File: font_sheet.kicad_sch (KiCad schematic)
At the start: 0 parts

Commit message: Troquei o micro para STM32H523, adicionei o cristal HSE, circuito da fonte de 5V e 3v3, CAN, SD
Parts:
- added C14, C15: 10u, Capacitor_THT:CP_Radial_D6.3mm_P2.50mm, symbol Device:C
- added C16: 10u, symbol Device:C
- added C17: 100n, symbol Device:C
- added D4: LED, BajaKICAD:LED_1210_HandSoldering, symbol Device:LED
- added R2: 1k, Resistor_SMD:R_1206_3216Metric_Pad1.30x1.75mm_HandSolder, symbol Device:R
- added U1: AMS1117-3.3, Package_TO_SOT_SMD:SOT-223-3_TabPin2, symbol Regulator_Linear:AMS1117-3.3
- added U11: AMS1117-5.0, Package_TO_SOT_SMD:SOT-223-3_TabPin2, symbol Regulator_Linear:AMS1117-5.0
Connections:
- new net: D4.2 (A), R2.2
- new net +12V: C16.1, U11.3 (VI)
- new net +3V3: C15.1, R2.1, U1.2 (VO)
- new net +5V: C14.1, C17.1, U1.3 (VI), U11.2 (VO)
- new net GND: C14.2, C15.2, C16.2, C17.2, D4.1 (K), U1.1 (GND), U11.1 (GND)
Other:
- note added: "Fonte 3V3 (LDO)"
- note added: "Fonte 5V (LDO)"
- note added: "LED da fonte"
- note added: "Nota: Capacitor "bulky" de desacoplamento é da entrada, o da saída já tem na fonte de 3v3"
- note added: "Nota: Compatível com LDL1117 da ST"

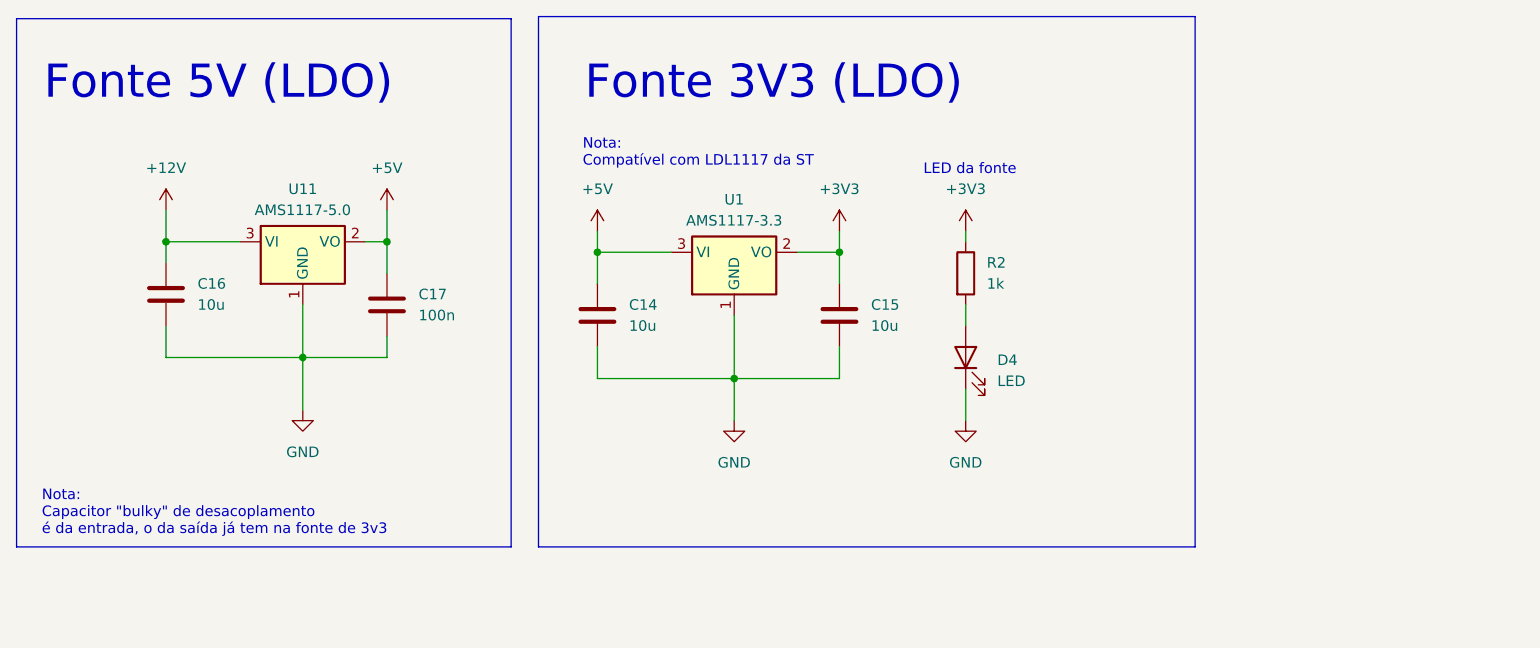
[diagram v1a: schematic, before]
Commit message: Alterei o nome para o par diferencial do CAN, adicionei capacitores de desacoplamento para todas as alimentacoes
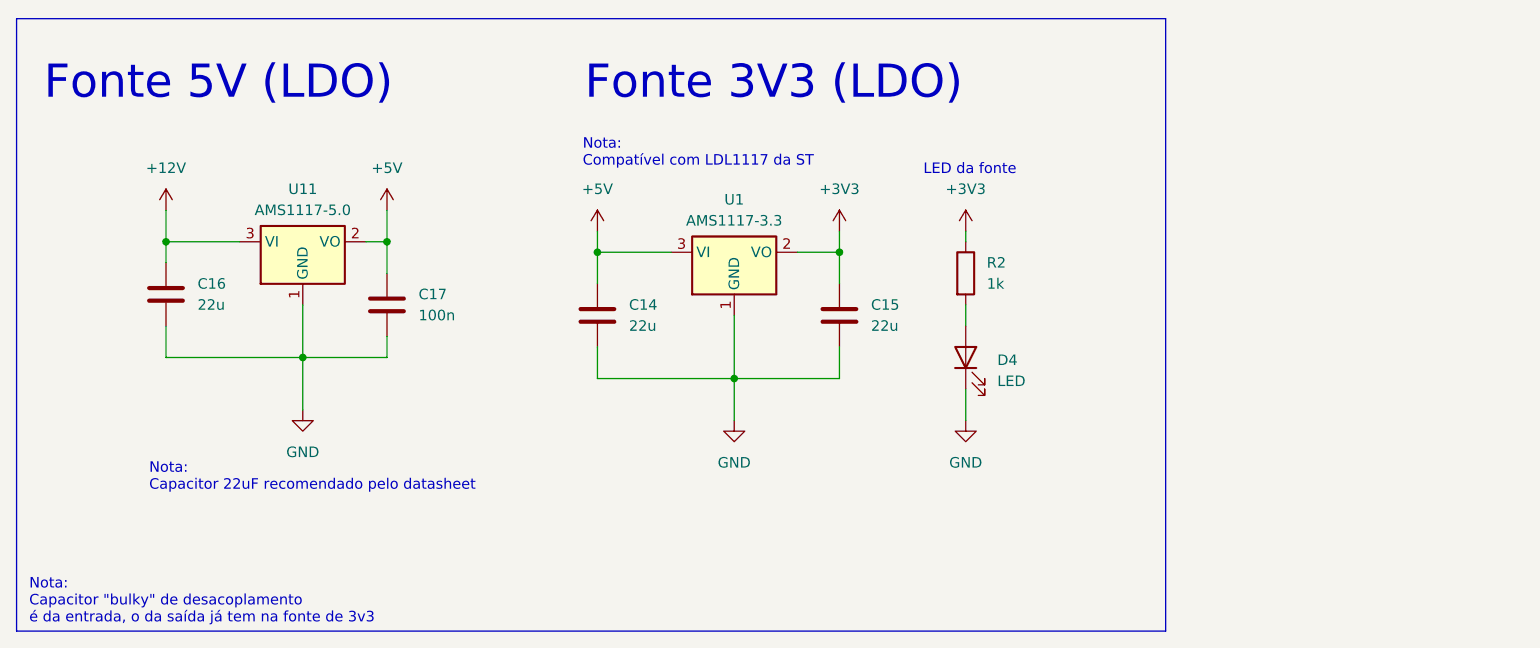
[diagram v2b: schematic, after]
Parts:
- C14, C15, C16: value 10u -> 22u
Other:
- note added: "Nota: Capacitor 22uF recomendado pelo datasheet"
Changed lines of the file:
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@@
 	(rectangle
 		(start 83.566 55.626)
-		(end 143.256 119.38)
-		(stroke
-			(width 0)
-			(type default)
-		)
-		(fill
-			(type none)
-		)
-	)
-	(rectangle
-		(start 146.558 55.372)
-		(end 225.806 119.38)
+		(end 222.25 129.54)
 		(stroke
 			(width 0)
@@
 	(text "Nota:\nCapacitor \"bulky\" de desacoplamento \né da entrada, o da saída já tem na fonte de 3v3"
 		(exclude_from_sim no)
-		(at 86.614 115.316 0)
+		(at 85.09 125.984 0)
+		(effects
+			(font
+				(size 1.27 1.27)
+			)
+			(justify left)
+		)
+	)
+	(text "Nota:\nCapacitor 22uF recomendado pelo datasheet"
+		(exclude_from_sim no)
+		(at 99.568 110.998 0)
 		(effects
 			(font
@@
 			)
 		)
-		(property "Value" "10u"
+		(property "Value" "22u"
 			(at 105.41 90.1699 0)
 			(effects
@@
 			)
 		)
-		(property "Value" "10u"
+		(property "Value" "22u"
 			(at 186.69 92.7099 0)
 			(effects
@@
 			)
 		)
-		(property "Value" "10u"
+		(property "Value" "22u"
 			(at 157.48 92.7099 0)
 			(effects

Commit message: Removi as entradas analógicas, projeto delas estava errado
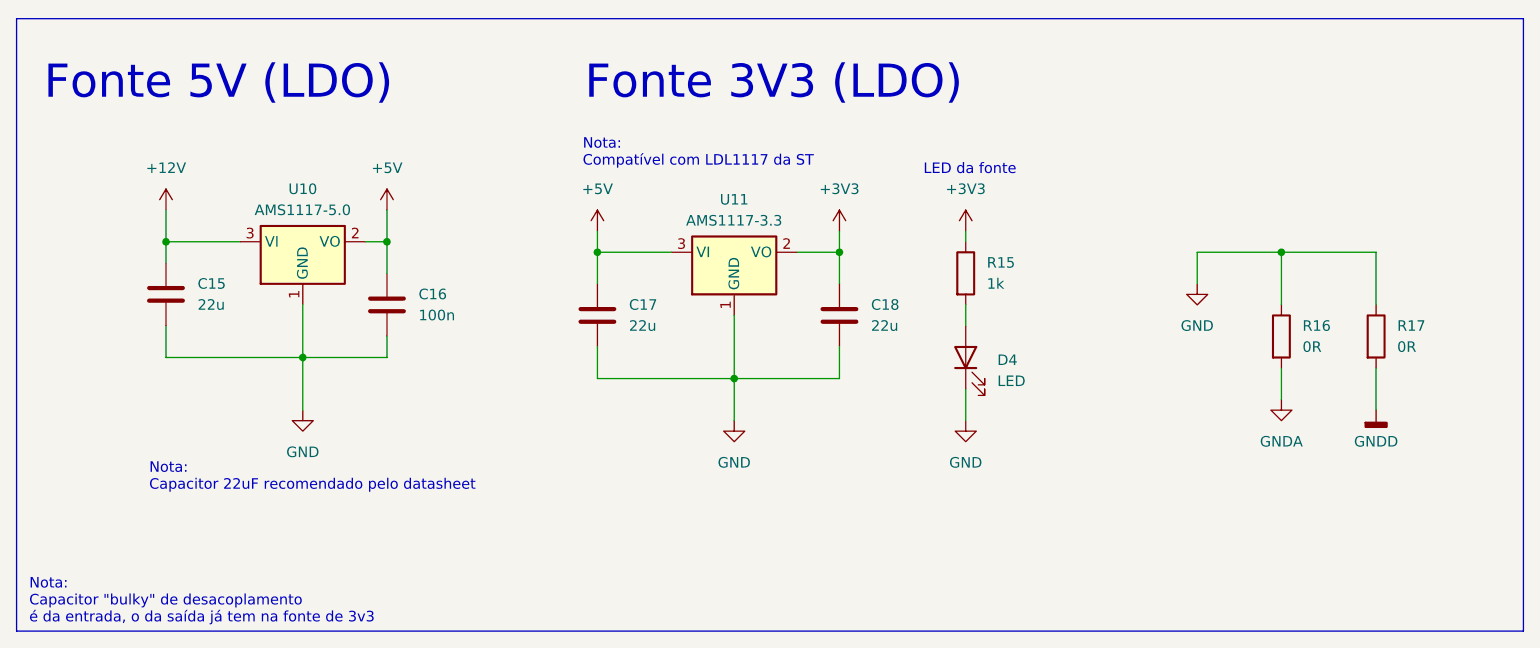
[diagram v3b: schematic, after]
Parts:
- added R16, R17: 0R, Baja_Library:JumperPotencia, symbol Device:R
- C15: renamed from C16; footprint (none) -> Capacitor_THT:CP_Radial_D6.3mm_P2.50mm
- C16: renamed from C17; footprint (none) -> Capacitor_SMD:C_0603_1608Metric_Pad1.08x0.95mm_HandSolder
- D4: footprint BajaKICAD:LED_1210_HandSoldering -> Baja_Library:LED_1210_HandSoldering
- renumbered C14 to C17, C15 to C18, R2 to R15, U11 to U10, U1 to U11
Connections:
- net GND: now also R16.1, R17.1
- new net GNDA: R16.2
- new net GNDD: R17.2
